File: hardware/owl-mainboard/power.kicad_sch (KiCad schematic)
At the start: 44 parts, among them J101 Battery +, NTC, -, U101 BQ24073RGTR, U102 MAX17048G+T10, U103 TPS63802DLAR, U104 TPS22917DBVR

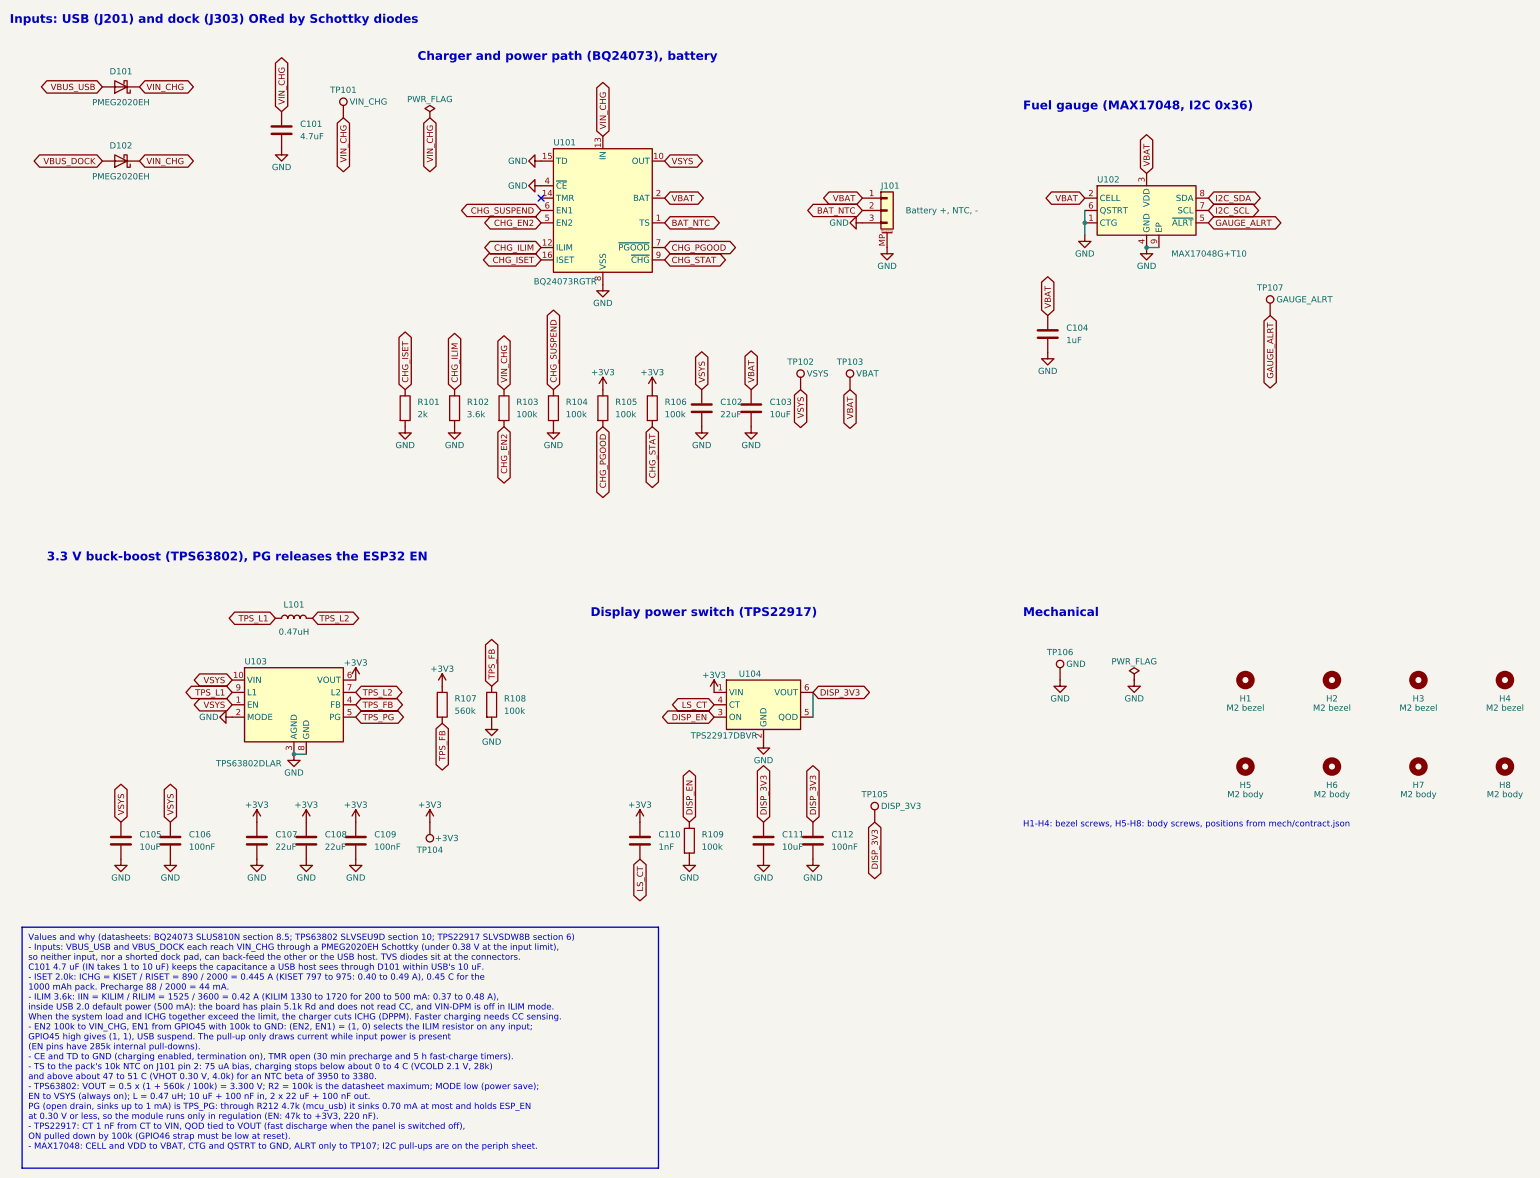
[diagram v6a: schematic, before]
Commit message: feat(hardware): put a 10k NTC on the board and make J101 a 2-pin JST PH
Cheap 803040 packs are 2-wire with a JST PH 2.0 plug, and the BQ24073
does not charge with TS open. J101 becomes the 2-pin S2B-PH-SM4-TB
(C295747; pin 1 VBAT, pin 2 GND) and RT101, a Murata NCP15XH103F03RC
(C77131, 10k 1 %, B25/50 3380 K, B25/85 3434 K: the 103AT-2 curve the TS
thresholds assume), goes between BAT_NTC and GND. No 10k NTC is Basic or
Preferred at JLC, so it is Extended.

hw_sync.py swapped J101 in place at its contract position and added
RT101; hw_place.py puts RT101 on the back under the cell at (-4, -9.5),
30 mm from U101, and draws + and - with a pin 1 dot beside J101's two
pins (the stale NTC mark goes). Pin 1 moved from y 16 to y 17, so the
charger's VBAT run and the fuel gauge's Kelvin tap follow it.
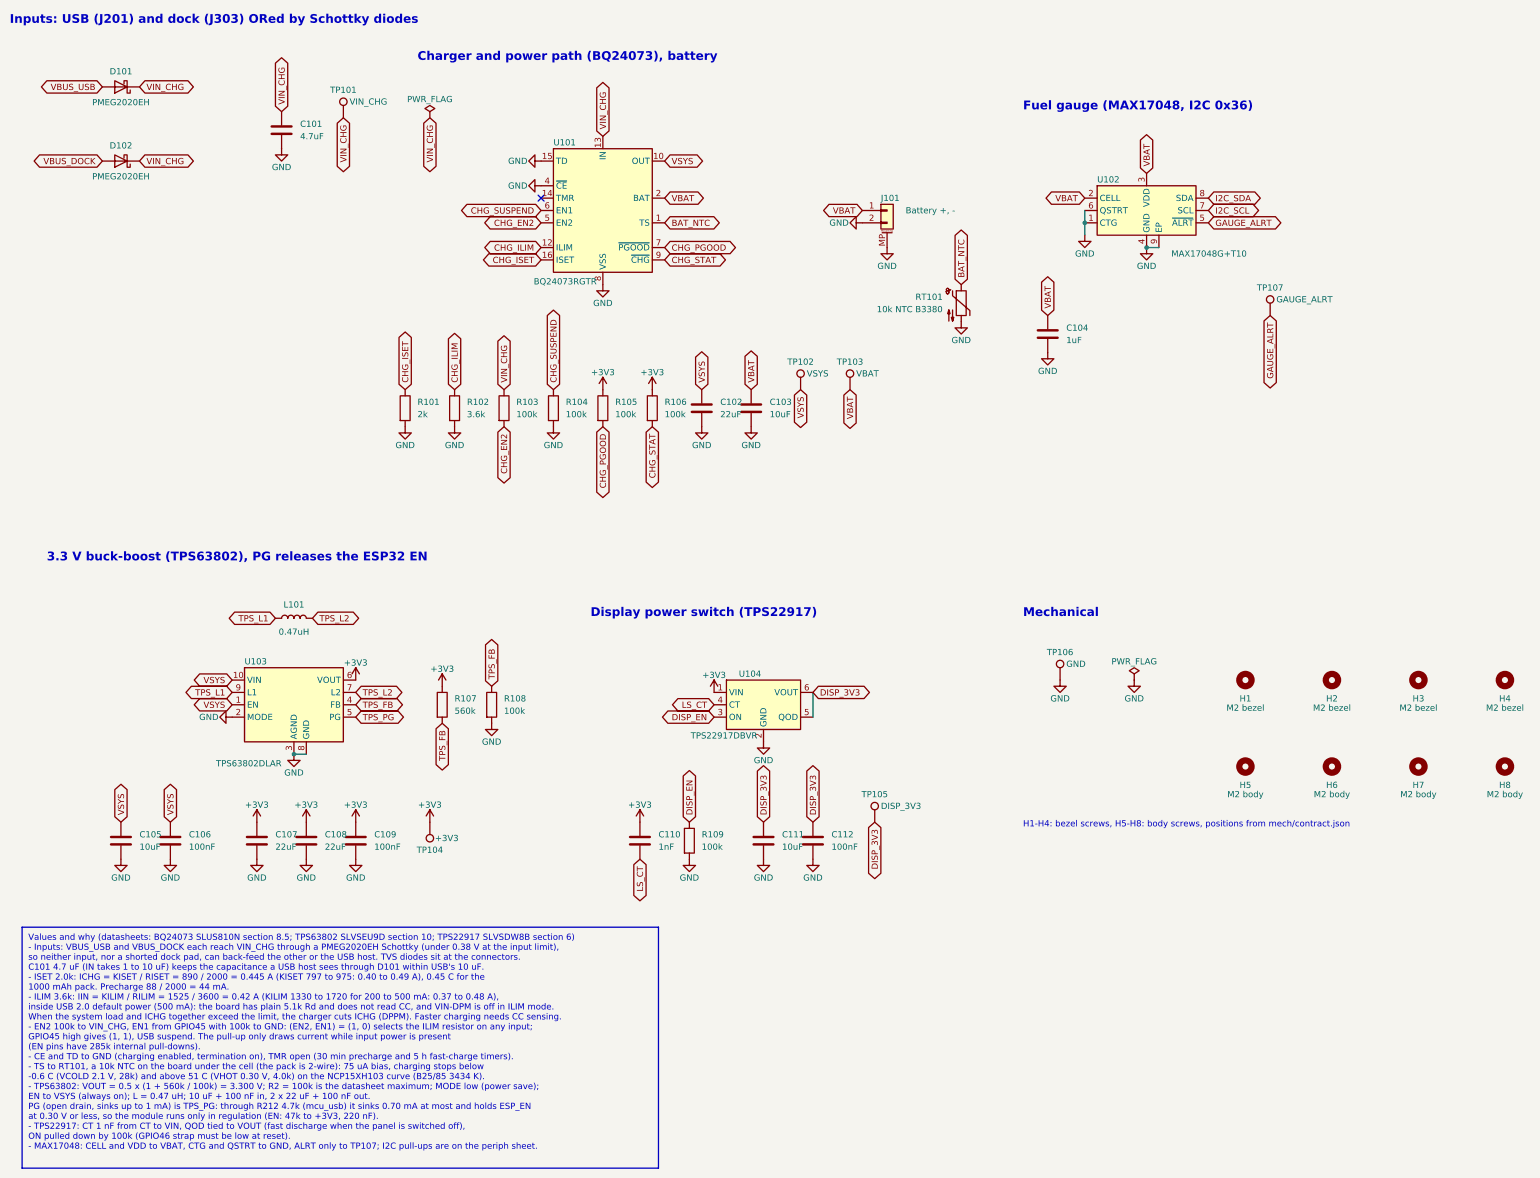
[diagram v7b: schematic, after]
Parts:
- added RT101: 10k NTC B3380, Resistor_SMD:R_0402_1005Metric, symbol Device:Thermistor_NTC
- J101: value Battery +, NTC, - -> Battery +, -; footprint Connector_JST:JST_PH_S3B-PH-SM4-TB_1x03-1MP_P2.00mm_Horizontal -> Connector_JST:JST_PH_S2B-PH-SM4-TB_1x02-1MP_P2.00mm_Horizontal; symbol Connector_Generic_MountingPin:Conn_01x03_MountingPin -> Connector_Generic_MountingPin:Conn_01x02_MountingPin; LCSC Part # C265101 -> C295747; MPN S3B-PH-SM4-TB(LF)(SN) -> S2B-PH-SM4-TB(LF)(SN)
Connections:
- net BAT_NTC: now also RT101.1; no longer J101.2 (Pin_2)
- net GND: now also J101.2 (Pin_2), RT101.2; no longer J101.3 (Pin_3)
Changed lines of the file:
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@@
 		)
 	)
-	(text_box "Values and why (datasheets: BQ24073 SLUS810N section 8.5; TPS63802 SLVSEU9D section 10; TPS22917 SLVSDW8B section 6)\n- Inputs: VBUS_USB and VBUS_DOCK each reach VIN_CHG through a PMEG2020EH Schottky (under 0.38 V at the input limit),\n  so neither input, nor a shorted dock pad, can back-feed the other or the USB host. TVS diodes sit at the connectors.\n  C101 4.7 uF (IN takes 1 to 10 uF) keeps the capacitance a USB host sees through D101 within USB's 10 uF.\n- ISET 2.0k: ICHG = KISET / RISET = 890 / 2000 = 0.445 A (KISET 797 to 975: 0.40 to 0.49 A), 0.45 C for the\n  1000 mAh pack. Precharge 88 / 2000 = 44 mA.\n- ILIM 3.6k: IIN = KILIM / RILIM = 1525 / 3600 = 0.42 A (KILIM 1330 to 1720 for 200 to 500 mA: 0.37 to 0.48 A),\n  inside USB 2.0 default power (500 mA): the board has plain 5.1k Rd and does not read CC, and VIN-DPM is off in ILIM mode.\n  When the system load and ICHG together exceed the limit, the charger cuts ICHG (DPPM). Faster charging needs CC sensing.\n- EN2 100k to VIN_CHG, EN1 from GPIO45 with 100k to GND: (EN2, EN1) = (1, 0) selects the ILIM resistor on any input;\n  GPIO45 high gives (1, 1), USB suspend. The pull-up only draws current while input power is present\n  (EN pins have 285k internal pull-downs).\n- CE and TD to GND (charging enabled, termination on), TMR open (30 min precharge and 5 h fast-charge timers).\n- TS to the pack's 10k NTC on J101 pin 2: 75 uA bias, charging stops below about 0 to 4 C (VCOLD 2.1 V, 28k)\n  and above about 47 to 51 C (VHOT 0.30 V, 4.0k) for an NTC beta of 3950 to 3380.\n- TPS63802: VOUT = 0.5 x (1 + 560k / 100k) = 3.300 V; R2 = 100k is the datasheet maximum; MODE low (power save);\n  EN to VSYS (always on); L = 0.47 uH; 10 uF + 100 nF in, 2 x 22 uF + 100 nF out.\n  PG (open drain, sinks up to 1 mA) is TPS_PG: through R212 4.7k (mcu_usb) it sinks 0.70 mA at most and holds ESP_EN\n  at 0.30 V or less, so the module runs only in regulation (EN: 47k to +3V3, 220 nF).\n- TPS22917: CT 1 nF from CT to VIN, QOD tied to VOUT (fast discharge when the panel is switched off),\n  ON pulled down by 100k (GPIO46 strap must be low at reset).\n- MAX17048: CELL and VDD to VBAT, CTG and QSTRT to GND, ALRT only to TP107; I2C pull-ups are on the periph sheet."
+	(text_box "Values and why (datasheets: BQ24073 SLUS810N section 8.5; TPS63802 SLVSEU9D section 10; TPS22917 SLVSDW8B section 6)\n- Inputs: VBUS_USB and VBUS_DOCK each reach VIN_CHG through a PMEG2020EH Schottky (under 0.38 V at the input limit),\n  so neither input, nor a shorted dock pad, can back-feed the other or the USB host. TVS diodes sit at the connectors.\n  C101 4.7 uF (IN takes 1 to 10 uF) keeps the capacitance a USB host sees through D101 within USB's 10 uF.\n- ISET 2.0k: ICHG = KISET / RISET = 890 / 2000 = 0.445 A (KISET 797 to 975: 0.40 to 0.49 A), 0.45 C for the\n  1000 mAh pack. Precharge 88 / 2000 = 44 mA.\n- ILIM 3.6k: IIN = KILIM / RILIM = 1525 / 3600 = 0.42 A (KILIM 1330 to 1720 for 200 to 500 mA: 0.37 to 0.48 A),\n  inside USB 2.0 default power (500 mA): the board has plain 5.1k Rd and does not read CC, and VIN-DPM is off in ILIM mode.\n  When the system load and ICHG together exceed the limit, the charger cuts ICHG (DPPM). Faster charging needs CC sensing.\n- EN2 100k to VIN_CHG, EN1 from GPIO45 with 100k to GND: (EN2, EN1) = (1, 0) selects the ILIM resistor on any input;\n  GPIO45 high gives (1, 1), USB suspend. The pull-up only draws current while input power is present\n  (EN pins have 285k internal pull-downs).\n- CE and TD to GND (charging enabled, termination on), TMR open (30 min precharge and 5 h fast-charge timers).\n- TS to RT101, a 10k NTC on the board under the cell (the pack is 2-wire): 75 uA bias, charging stops below\n  -0.6 C (VCOLD 2.1 V, 28k) and above 51 C (VHOT 0.30 V, 4.0k) on the NCP15XH103 curve (B25/85 3434 K).\n- TPS63802: VOUT = 0.5 x (1 + 560k / 100k) = 3.300 V; R2 = 100k is the datasheet maximum; MODE low (power save);\n  EN to VSYS (always on); L = 0.47 uH; 10 uF + 100 nF in, 2 x 22 uF + 100 nF out.\n  PG (open drain, sinks up to 1 mA) is TPS_PG: through R212 4.7k (mcu_usb) it sinks 0.70 mA at most and holds ESP_EN\n  at 0.30 V or less, so the module runs only in regulation (EN: 47k to +3V3, 220 nF).\n- TPS22917: CT 1 nF from CT to VIN, QOD tied to VOUT (fast discharge when the panel is switched off),\n  ON pulled down by 100k (GPIO46 strap must be low at reset).\n- MAX17048: CELL and VDD to VBAT, CTG and QSTRT to GND, ALRT only to TP107; I2C pull-ups are on the periph sheet."
 		(exclude_from_sim no)
 		(at 20.32 223.52 0)
@@
 	(global_label "BAT_NTC"
 		(shape bidirectional)
-		(at 193.04 76.2 180)
+		(at 213.36 91.44 90)
 		(effects
 			(font
 				(size 1.27 1.27)
 			)
-			(justify right)
+			(justify left)
 		)
 		(property "Intersheetrefs" "${INTERSHEET_REFS}"
-			(at 193.04 76.2 0)
+			(at 213.36 91.44 0)
 			(hide yes)
 			(show_name no)
@@
 	(global_label "VBAT"
 		(shape bidirectional)
-		(at 193.04 73.66 180)
+		(at 193.04 76.2 180)
 		(effects
 			(font
@@
 		)
 		(property "Intersheetrefs" "${INTERSHEET_REFS}"
-			(at 193.04 73.66 0)
+			(at 193.04 76.2 0)
 			(hide yes)
 			(show_name no)
@@
 	)
 	(symbol
-		(lib_id "Connector_Generic_MountingPin:Conn_01x03_MountingPin")
+		(lib_id "Connector_Generic_MountingPin:Conn_01x02_MountingPin")
 		(at 198.12 76.2 0)
 		(unit 1)
@@
 		(dnp no)
 		(property "Reference" "J101"
-			(at 196.85 71.12 0)
+			(at 196.85 73.66 0)
 			(show_name no)
 			(do_not_autoplace no)
@@
 			)
 		)
-		(property "Value" "Battery +, NTC, -"
+		(property "Value" "Battery +, -"
 			(at 201.93 76.2 0)
 			(show_name no)
@@
 			)
 		)
-		(property "Footprint" "Connector_JST:JST_PH_S3B-PH-SM4-TB_1x03-1MP_P2.00mm_Horizontal"
+		(property "Footprint" "Connector_JST:JST_PH_S2B-PH-SM4-TB_1x02-1MP_P2.00mm_Horizontal"
 			(at 198.12 76.2 0)
 			(hide yes)
@@
 			)
 		)
-		(property "Description" "Generic connectable mounting pin connector, single row, 01x03, script generated (kicad-library-utils/schlib/autogen/connector/)"
+		(property "Description" "Generic connectable mounting pin connector, single row, 01x02, script generated (kicad-library-utils/schlib/autogen/connector/)"
 			(at 198.12 76.2 0)
 			(hide yes)
@@
 			)
 		)
-		(property "LCSC Part #" "C265101"
+		(property "LCSC Part #" "C295747"
 			(at 198.12 76.2 0)
 			(hide yes)
@@
 			)
 		)
-		(property "MPN" "S3B-PH-SM4-TB(LF)(SN)"
+		(property "MPN" "S2B-PH-SM4-TB(LF)(SN)"
 			(at 198.12 76.2 0)
 			(hide yes)
@@
 		(pin "2"
 		)
-		(pin "3"
-		)
 		(pin "MP"
 		)
@@
 					(unit 1)
 				)
+			)
+		)
+	)
+	(symbol
+		(lib_id "Device:Thermistor_NTC")
+		(at 213.36 95.25 0)
+		(unit 1)
+		(body_style 1)
+		(exclude_from_sim no)
+		(in_bom yes)
+		(on_board yes)
+		(in_pos_files yes)
+		(dnp no)
+		(property "Reference" "RT101"
+			(at 209.55 93.98 0)
+			(show_name no)
+			(do_not_autoplace no)
+			(effects
+				(font
+					(size 1.27 1.27)
+				)
+				(justify right)
+			)
+		)
+		(property "Value" "10k NTC B3380"
+			(at 209.55 96.52 0)
+			(show_name no)
+			(do_not_autoplace no)
+			(effects
+				(font
+					(size 1.27 1.27)
+				)
+				(justify right)
+			)
+		)
+		(property "Footprint" "Resistor_SMD:R_0402_1005Metric"
+			(at 213.36 95.25 0)
+			(hide yes)
+			(show_name no)
+			(do_not_autoplace no)
+			(effects
+				(font
+					(size 1.27 1.27)
+				)
+			)
+		)
+		(property "Datasheet" ""
+			(at 213.36 95.25 0)
+			(hide yes)
+			(show_name no)
+			(do_not_autoplace no)
+			(effects
+				(font
+					(size 1.27 1.27)
+				)
+			)
+		)
+		(property "Description" "Temperature dependent resistor, negative temperature coefficient"
+			(at 213.36 95.25 0)
+			(hide yes)
+			(show_name no)
+			(do_not_autoplace no)
+			(effects
+				(font
+					(size 1.27 1.27)
+				)
+			)
+		)
+		(property "LCSC Part #" "C77131"
+			(at 213.36 95.25 0)
+			(hide yes)
+			(show_name no)
+			(do_not_autoplace no)
+			(effects
+				(font
+					(size 1.27 1.27)
+				)
+			)
+		)
+		(property "MPN" "NCP15XH103F03RC"
+			(at 213.36 95.25 0)
+			(hide yes)
+			(show_name no)
+			(do_not_autoplace no)
+			(effects
+				(font
+					(size 1.27 1.27)
+				)
+			)
+		)
+		(property "Manufacturer" "Murata Electronics"
+			(at 213.36 95.25 0)
+			(hide yes)
+			(show_name no)
+			(do_not_autoplace no)
+			(effects
+				(font
+					(size 1.27 1.27)
+				)
+			)
+		)
+		(pin "1"
+		)
+		(pin "2"
+		)
+		(instances
+			(project "owl-mainboard"
+				(path "/fb846a48-d7cd-4e1f-898e-fc44b04beae7/4af1d6fc-f0db-4f00-b9e9-54eaa77529fa"
+					(reference "RT101")
+					(unit 1)
+				)
+			)
+		)
+	)
+	(symbol
+		(lib_id "power:GND")
+		(at 213.36 99.06 0)
+		(unit 1)
+		(body_style 1)
+		(exclude_from_sim no)
+		(in_bom yes)
+		(on_board yes)
+		(in_pos_files yes)
+		(dnp no)
+		(property "Reference" "#PWR0139"
+			(at 213.36 92.71 0)
+			(hide yes)
+			(show_name no)
+			(do_not_autoplace no)
+			(effects
+				(font
+					(size 1.27 1.27)
+				)
+			)
+		)
+		(property "Value" "GND"
+			(at 213.36 102.87 0)
+			(show_name no)
+			(do_not_autoplace no)
+			(effects
+				(font
+					(size 1.27 1.27)
+				)
+			)
+		)
+		(property "Footprint" ""
+			(at 213.36 99.06 0)
+			(hide yes)
+			(show_name no)
+			(do_not_autoplace no)
+			(effects
+				(font
+					(size 1.27 1.27)
+				)
+			)
+		)
+		(property "Datasheet" ""
+			(at 213.36 99.06 0)
+			(hide yes)
+			(show_name no)
+			(do_not_autoplace no)
+			(effects
+				(font
+					(size 1.27 1.27)
+				)
+			)
+		)
+		(property "Description" "Power symbol creates a global label with name \"GND\" , ground"
+			(at 213.36 99.06 0)
+			(hide yes)
+			(show_name no)
+			(do_not_autoplace no)
+			(effects
+				(font
+					(size 1.27 1.27)
+				)
+			)
+		)
+		(pin "1"
+		)
+		(instances
+			(project "owl-mainboard"
+				(path "/fb846a48-d7cd-4e1f-898e-fc44b04beae7/4af1d6fc-f0db-4f00-b9e9-54eaa77529fa"
+					(reference "#PWR0139")
+					(unit 1)
+				)
